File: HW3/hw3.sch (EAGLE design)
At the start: 23 parts, among them J1 USB-MINIB-5PUSB-MINIB-2SUPPORT, J2 M06, J3 M08#1, J4 M08#2

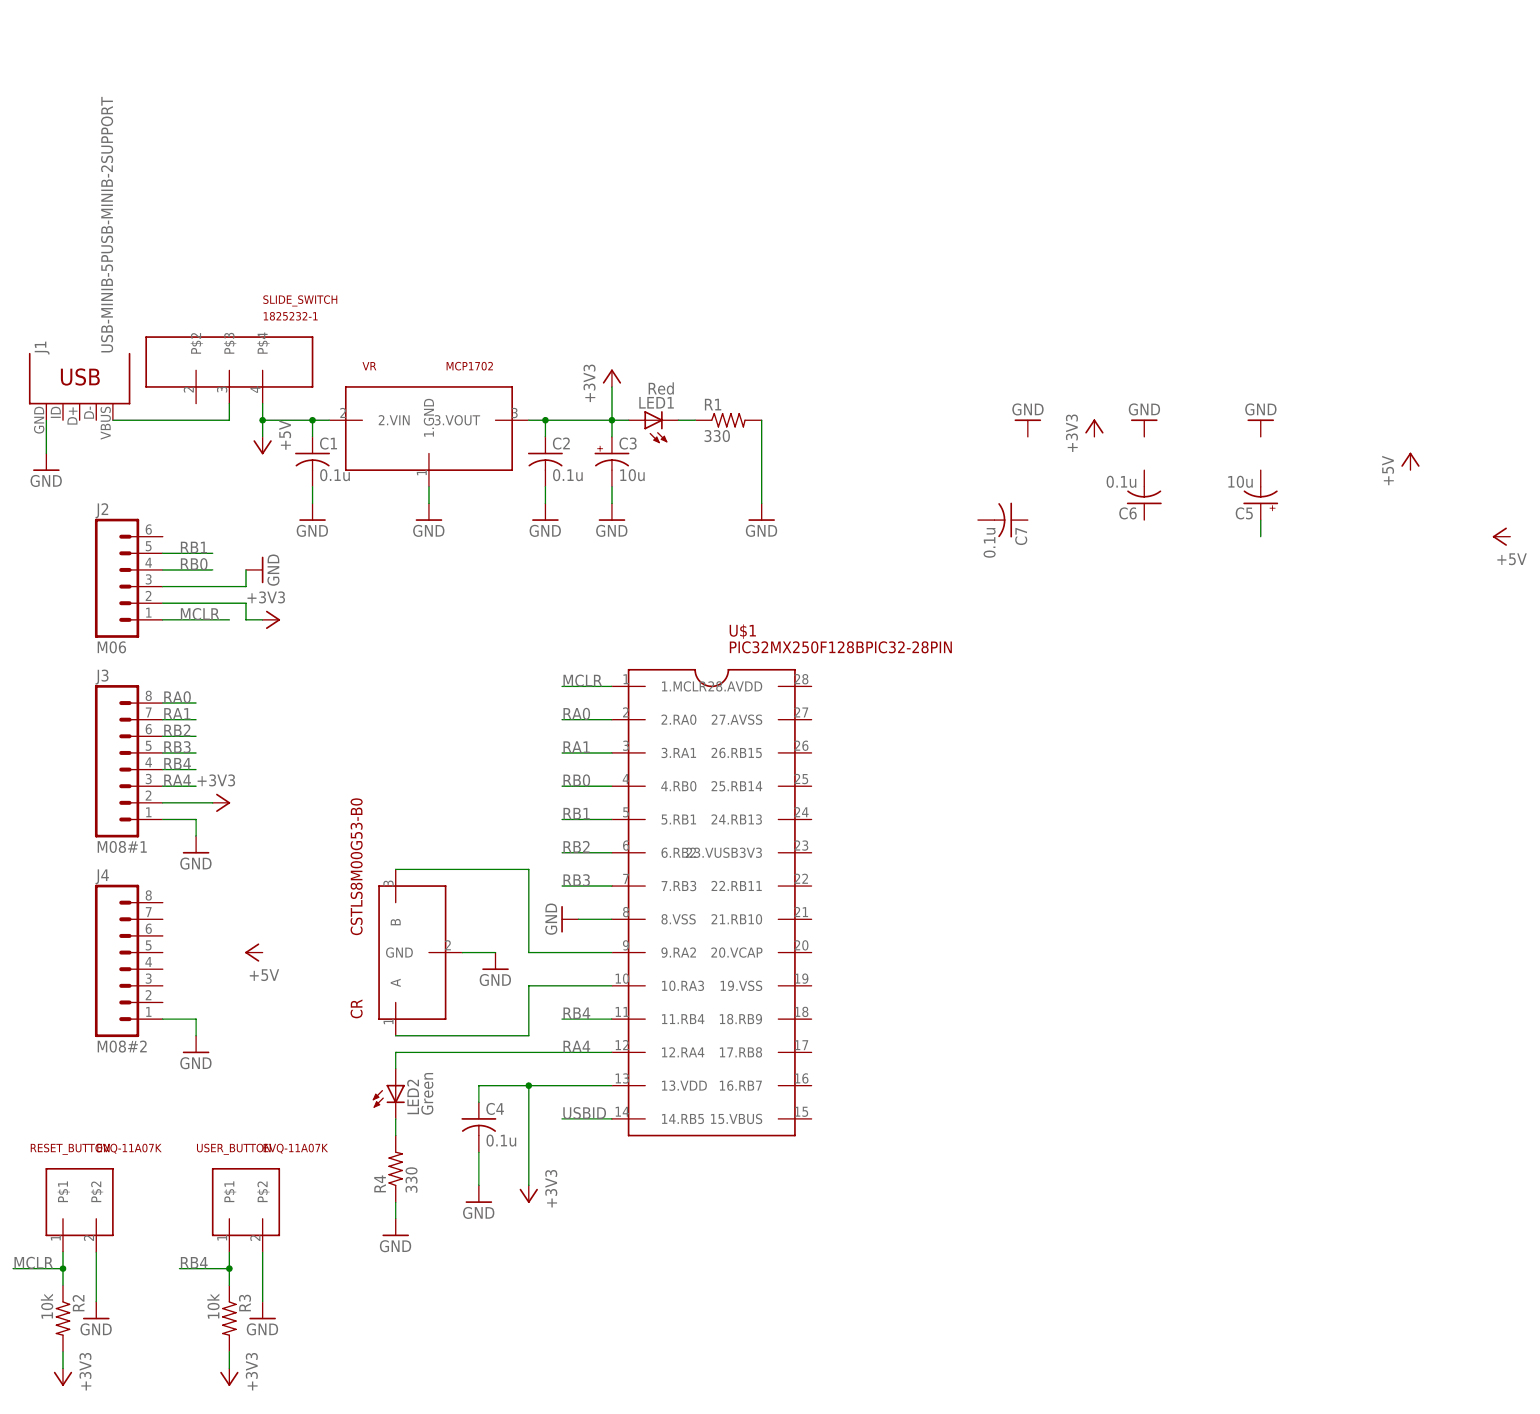
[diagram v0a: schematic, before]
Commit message: Redesigned schematic and board
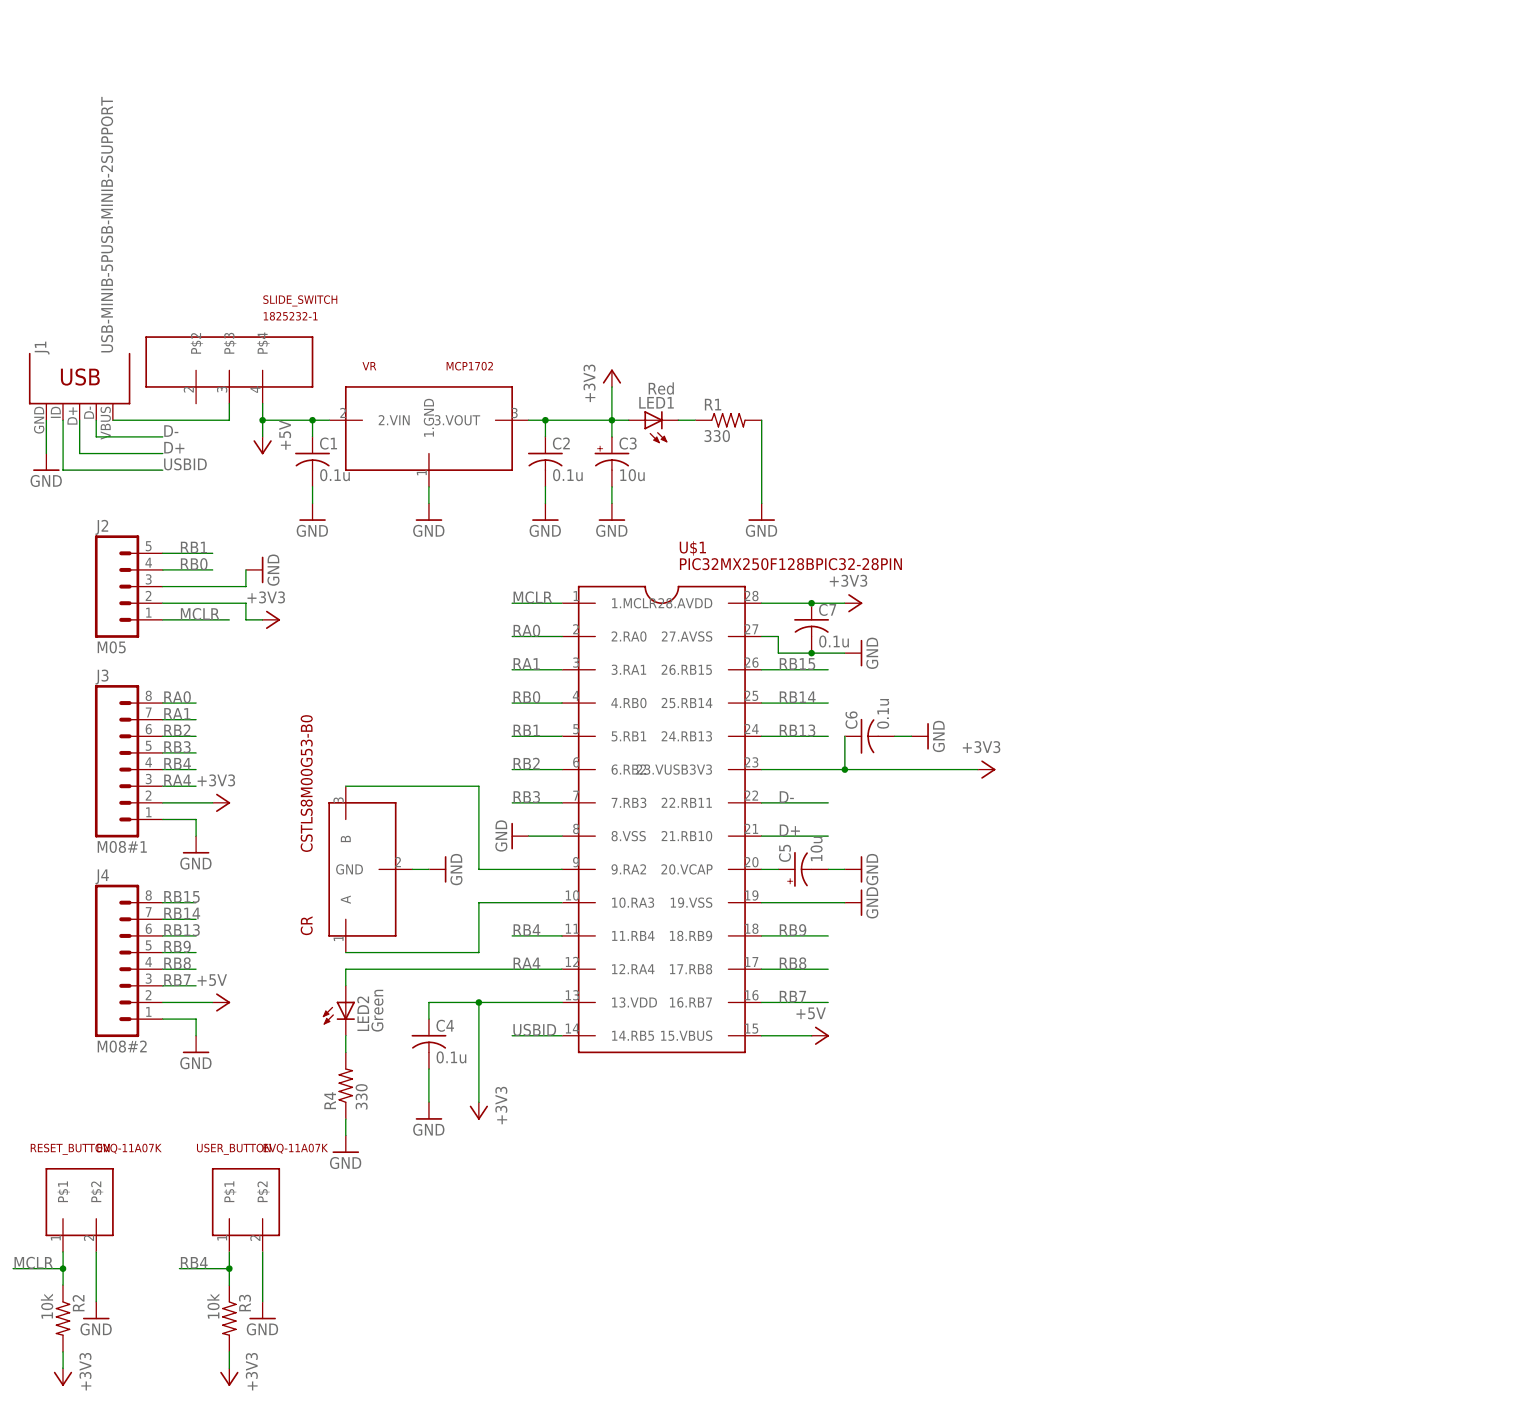
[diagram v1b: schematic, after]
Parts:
- J2: value M06 -> M05; device hw2:M06SILK_FEMALE_PTH -> hw2:M05NO_SILK
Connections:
- removed net N$14: C5.+
- new net D+: J1.D+, U$1.21.RB10
- new net D-: J1.D-, U$1.22.RB11
- new net N$2: C5.+, U$1.20.VCAP
- new net RB13: J4.6, U$1.24.RB13
- new net RB14: J4.7, U$1.25.RB14
- new net RB15: J4.8, U$1.26.RB15
- new net RB7: J4.3, U$1.16.RB7
- new net RB8: J4.4, U$1.17.RB8
- new net RB9: J4.5, U$1.18.RB9
- net +3V3: now also C6.1, C7.1, U$1.23.VUSB3V3, U$1.28.AVDD
- net +5V: now also J4.2, U$1.15.VBUS
- net GND: now also C5.-, C6.2, C7.2, U$1.19.VSS, U$1.27.AVSS
- net USBID: now also J1.ID
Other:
- moved on the sheet: C4, C5, C6, C7, CR, LED2, R4, U$1
